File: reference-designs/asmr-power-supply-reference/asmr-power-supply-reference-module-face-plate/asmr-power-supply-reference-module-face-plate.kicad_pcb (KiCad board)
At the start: 2 copper layers, 40 x 159.8 mm, 0 parts

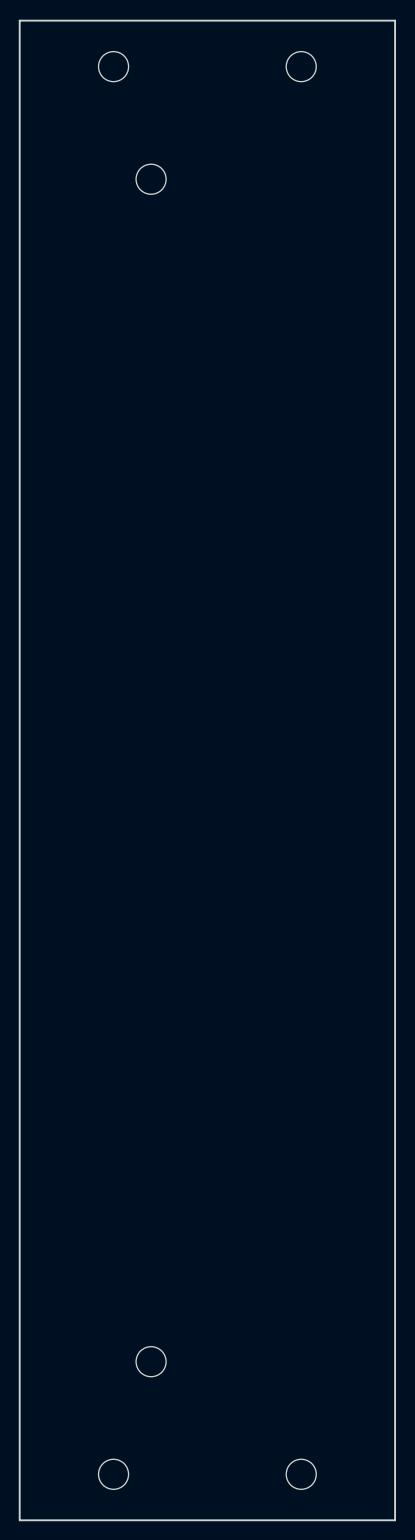
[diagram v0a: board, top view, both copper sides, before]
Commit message: Create faceplate for ASMR power supply module.
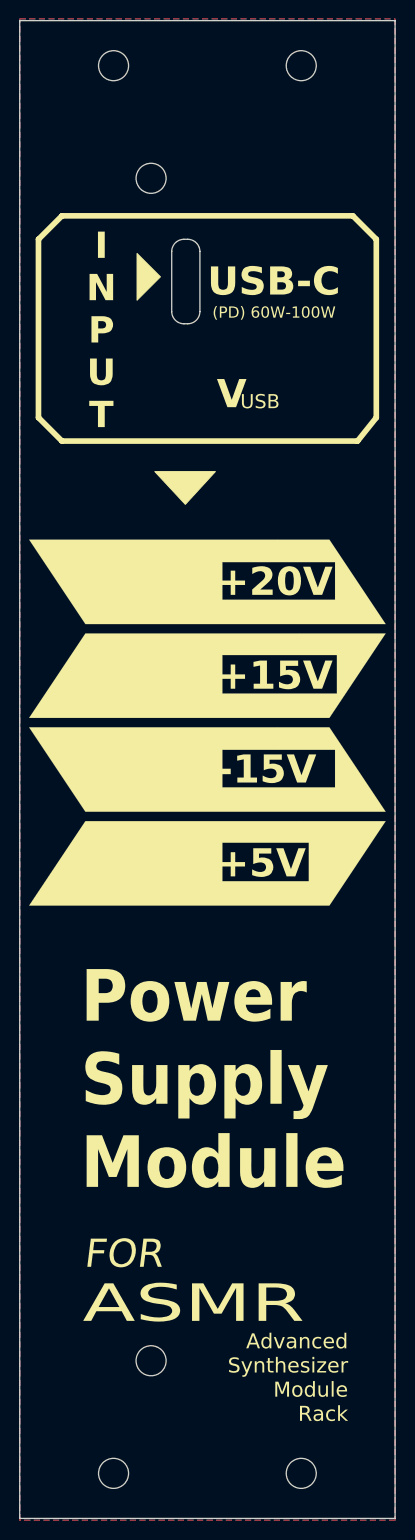
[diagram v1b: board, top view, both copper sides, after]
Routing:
- added copper zone on B.Cu, net (none)
- added copper zone on F.Cu, net (none)
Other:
- board size 40 x 159.8 mm -> 40 x 159.6 mm
- board text added: "(PD) 60W-100W"
- board text added: "+15V"
- board text added: "+20V"
- board text added: "+5V"
- board text added: "-15V"
- board text added: "ASMR"
- board text added: "Advanced Synthesizer Module Rack"
- board text added: "Component Side (PCB Front)"
- board text added: "FOR"
- board text added: "I N P U T"
- board text added: "LED"
- board text added: "Power Supply Module"
- board text added: "USB"
- board text added: "USB-C"
- board text added: "V"

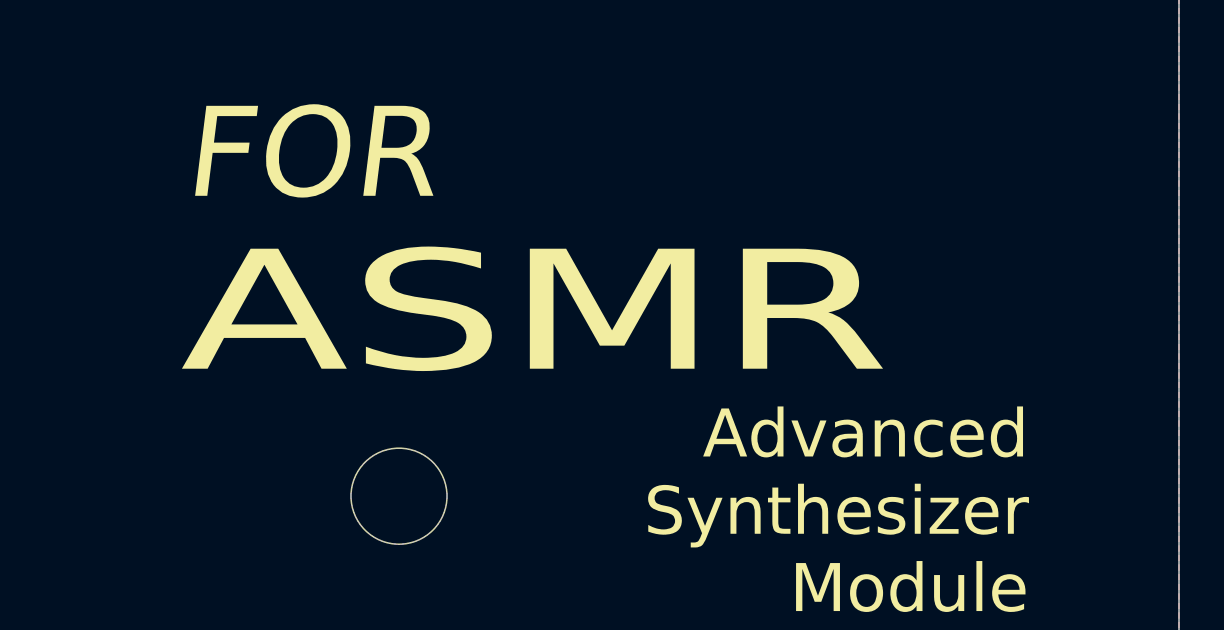
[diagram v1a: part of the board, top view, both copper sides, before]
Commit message: Tune Aesthetic of face plate.
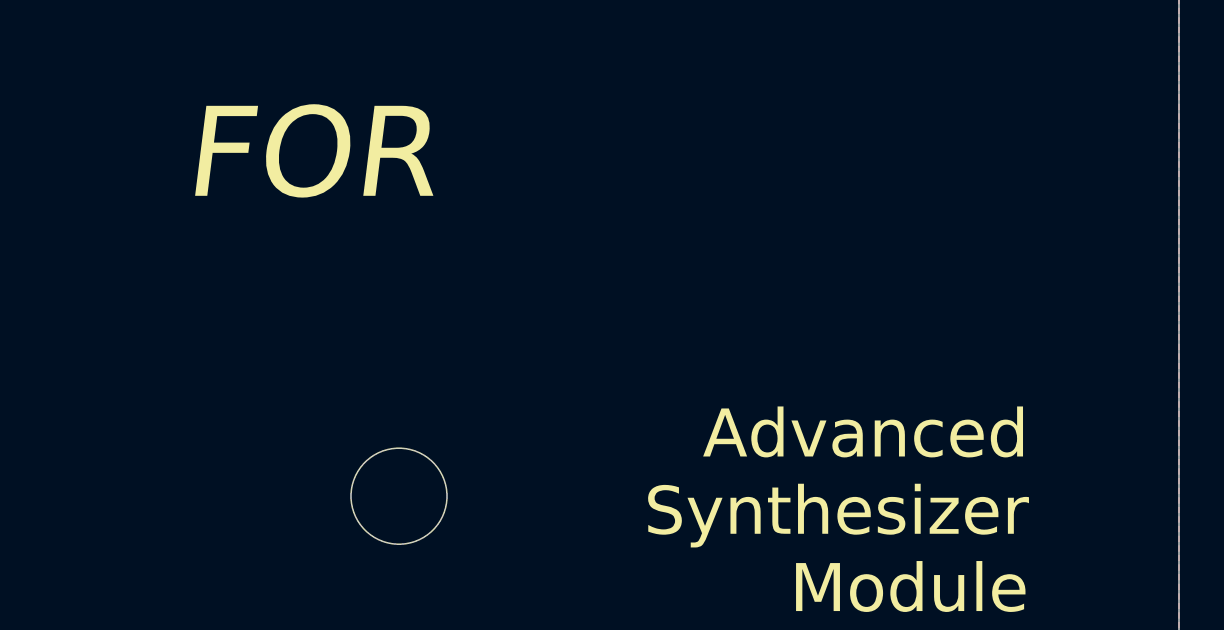
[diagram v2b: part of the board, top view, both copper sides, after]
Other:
- board text added: "A S M R"

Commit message: Add JLC PCB serial tag to back of PCB
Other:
- board text added: "JLCJLCJLCJLC"
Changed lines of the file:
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@@
+		)
+	)
+	(gr_text "JLCJLCJLCJLC"
+		(at 109 208 0)
+		(layer "B.SilkS")
+		(effects
+			(font
+				(size 1 1)
+				(thickness 0.1)
+			)
+			(justify mirror)
 		)
 	)
